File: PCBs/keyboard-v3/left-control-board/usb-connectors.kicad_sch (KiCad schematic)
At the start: 12 parts, among them J101 USB4510-03-1-A, J102 USB4510-03-1-A, J103 GSB12J21C1EU, J201 USB4510-03-1-A, U104 USBLC6-4SC6, U201 USBLC6-4SC6

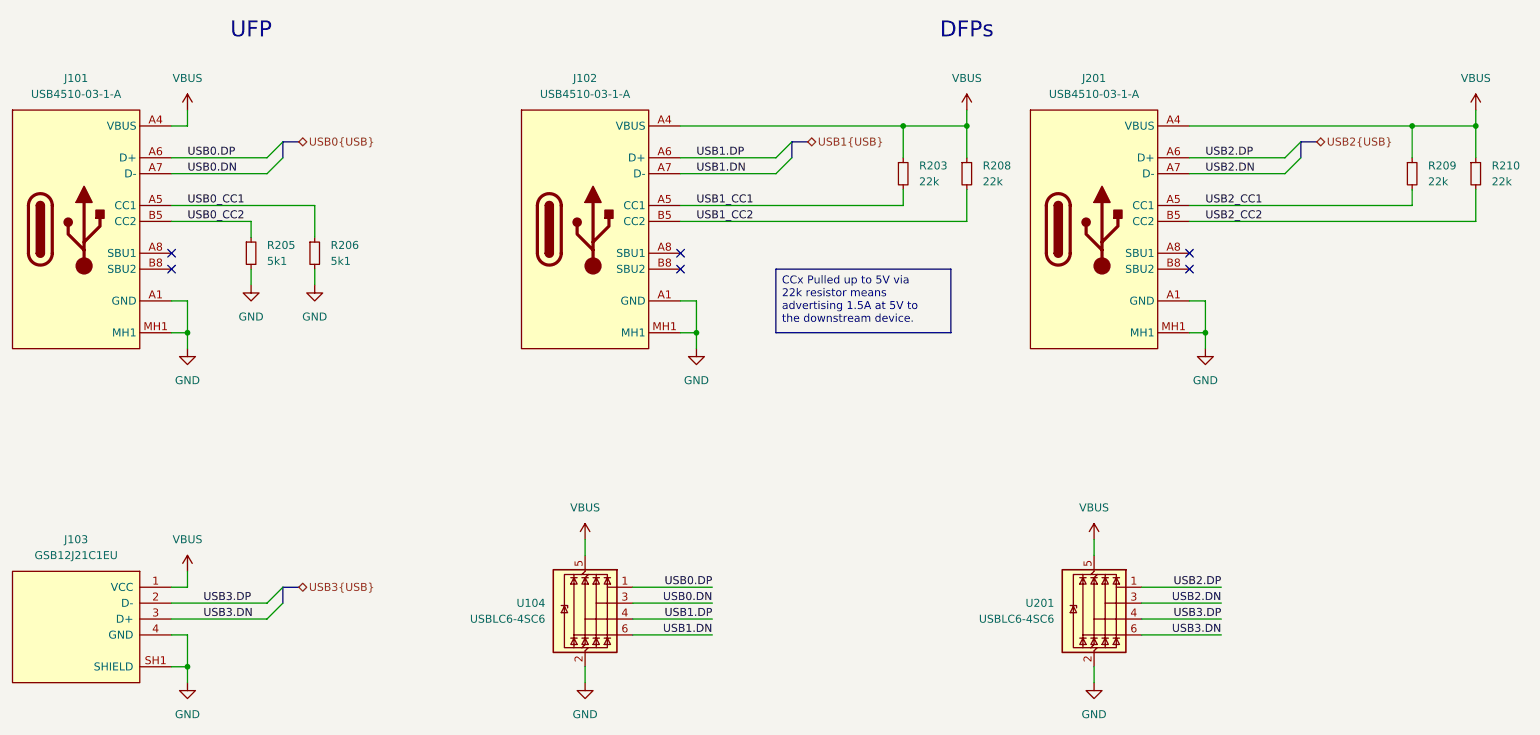
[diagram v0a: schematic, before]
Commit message: Added debug-breakout board, progress on right side schematics & layout
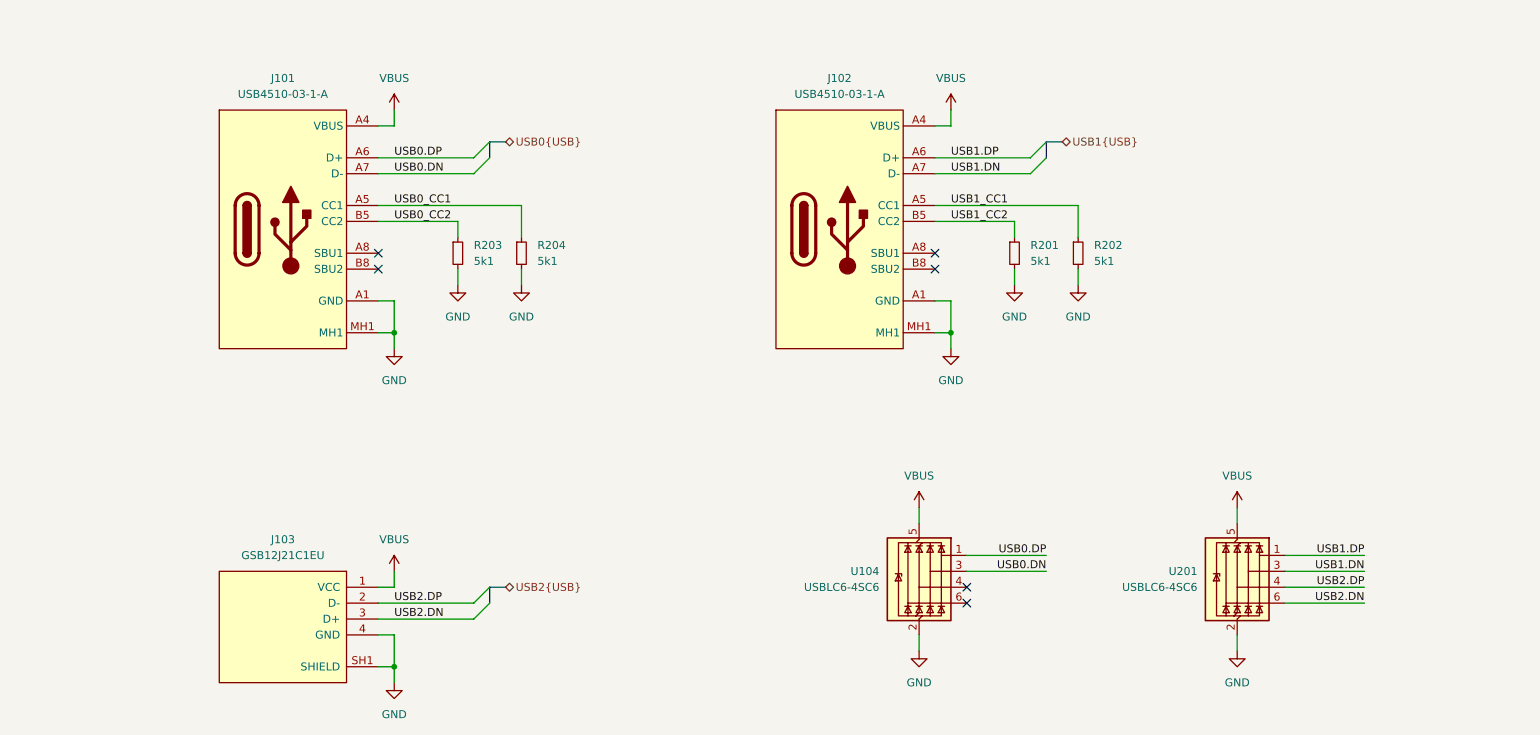
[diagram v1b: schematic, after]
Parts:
- removed J201: USB4510-03-1-A, project_footprints:USB4510031A, symbol USB-CONN:USB4510-03-1-A
- removed R205, R206: 5k1, project_footprints:R_0402, symbol DEV:R_SMALL
- removed R208, R209, R210: 22k, project_footprints:R_0402, symbol DEV:R_SMALL
- added R201, R202, R204: 5k1, project_footprints:R_0402, symbol DEV:R_SMALL
- R203: value 22k -> 5k1
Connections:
- net USB3.DN is gone; now on net USB2.DN: J103.3 (D+), U201.6 (I/O4)
- net USB3.DP is gone; now on net USB2.DP: J103.2 (D-), U201.4 (I/O3)
- net GND: now also R203.2, R201.2, R202.2, R204.2
- net USB0_CC1: now also R204.1
- net USB0_CC2: now also R203.1
- net USB1.DN: now also U201.3 (I/O2); no longer U104.6 (I/O4)
- net USB1.DP: now also U201.1 (I/O1); no longer U104.4 (I/O3)
- net USB1_CC1: now also R202.1; no longer R203.2
- net USB1_CC2: now also R201.1
- net USB2.DN: no longer U201.3 (I/O2)
- net USB2.DP: no longer U201.1 (I/O1)
- net VBUS: no longer R203.1
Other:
- note removed: "DFPs"
- note removed: "UFP"
- moved on the sheet: J101, J102, J103, U104, U201

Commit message: Left knob board done
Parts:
- removed R203, R204: 5k1, project_footprints:R_0402, symbol DEV:R_SMALL
- added R205, R206: 5k1, project_footprints:R_0402, symbol DEV:R_SMALL
- R201, R202: value 5k1 -> 22k
- renumbered J101 to J201, J102 to J202, J103 to J204, U104 to U201, U201 to U202
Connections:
- net GND: now also R205.2, R206.2; no longer R201.2, R202.2
- net USB0.DN: now also U202.3 (I/O2); no longer U201.3 (I/O2)
- net USB0.DP: now also U202.1 (I/O1); no longer U201.1 (I/O1)
- net USB0_CC1: now also R206.1
- net USB0_CC2: now also R205.1
- net USB1.DN: now also U201.4 (I/O3); no longer U202.3 (I/O2)
- net USB1.DP: now also U201.6 (I/O4); no longer U202.1 (I/O1)
- net USB1_CC1: now also R201.2; no longer R202.1
- net USB1_CC2: now also R202.2; no longer R201.1
- net VBUS: now also R201.1, R202.1
- net USB2.DN: no longer names the net of U202.6 (I/O4)
- net USB2.DN: no longer J204.3 (D+)
- net USB2.DP: no longer names the net of U202.4 (I/O3)
- net USB2.DP: no longer J204.2 (D-)
- new net USB3.DN: J204.3 (D+), U201.3 (I/O2)
- new net USB3.DP: J204.2 (D-), U201.1 (I/O1)
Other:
- note added: "DFP"
- note added: "UFP"
- moved on the sheet: J202, J204, U201, U202

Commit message: Keyboard v3 hardware done
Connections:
- net USB1.DN renamed USB2.DN
- net USB1.DP renamed USB2.DP
- net USB1_CC1 renamed USB2_CC1
- net USB1_CC2 renamed USB2_CC2
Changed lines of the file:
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@@
 		)
 	)
-	(label "USB1.DP"
+	(label "USB2.DP"
 		(at 175.26 60.96 0)
 		(effects
@@
 		)
 	)
-	(label "USB1.DP"
+	(label "USB2.DP"
 		(at 162.56 137.16 180)
 		(effects
@@
 			)
 			(justify right bottom)
-		)
-	)
-	(label "USB1.DN"
-		(at 175.26 63.5 0)
-		(effects
-			(font
-				(size 1.27 1.27)
-			)
-			(justify left bottom)
 		)
 	)
@@
 		)
 	)
-	(label "USB1_CC2"
+	(label "USB2.DN"
+		(at 175.26 63.5 0)
+		(effects
+			(font
+				(size 1.27 1.27)
+			)
+			(justify left bottom)
+		)
+	)
+	(label "USB2_CC2"
 		(at 175.26 71.12 0)
 		(effects
@@
 		)
 	)
-	(label "USB1.DN"
+	(label "USB2.DN"
 		(at 162.56 134.62 180)
 		(effects
@@
 		)
 	)
-	(label "USB1_CC1"
+	(label "USB2_CC1"
 		(at 175.26 68.58 0)
 		(effects
@@
 		)
 	)
-	(hierarchical_label "USB1{USB}"
+	(hierarchical_label "USB2{USB}"
 		(shape bidirectional)
 		(at 193.04 58.42 0)
